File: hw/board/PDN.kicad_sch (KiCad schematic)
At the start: 40 parts, among them U1 XC7A35T-FTG256

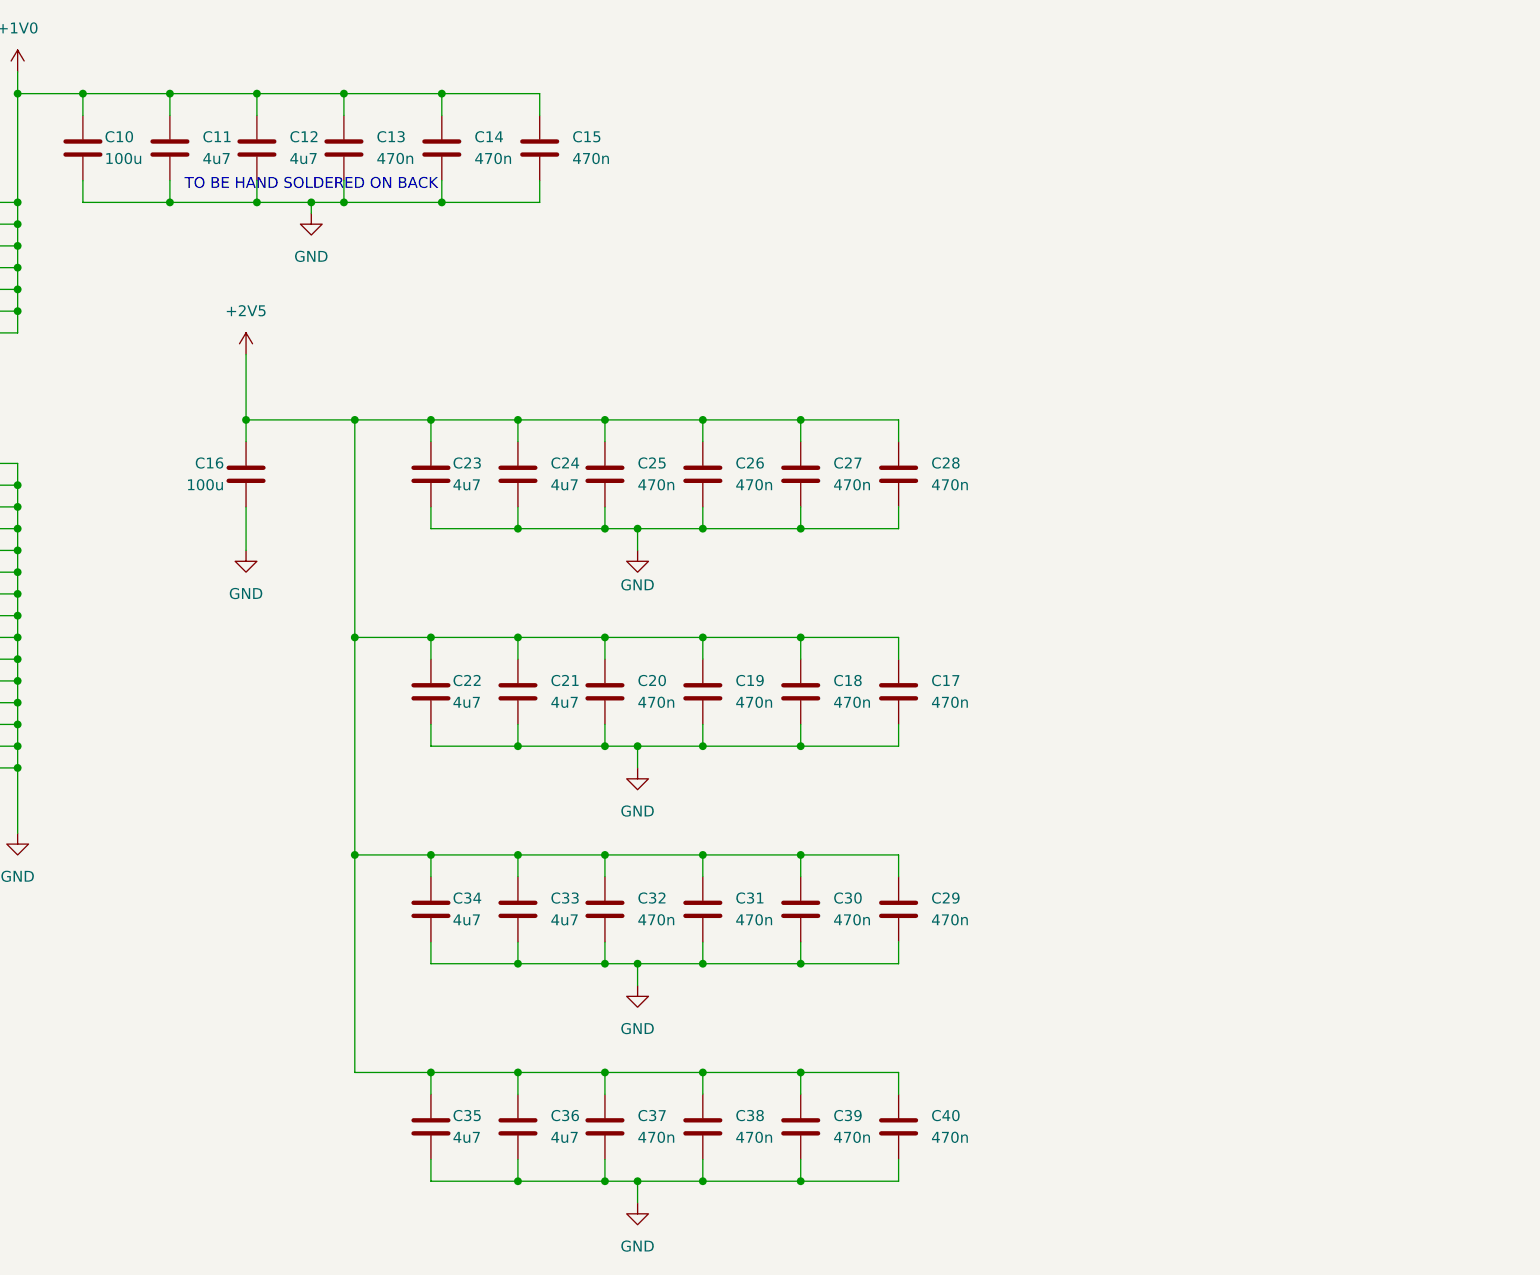
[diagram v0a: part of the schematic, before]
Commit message: Routed DE-9 connectors
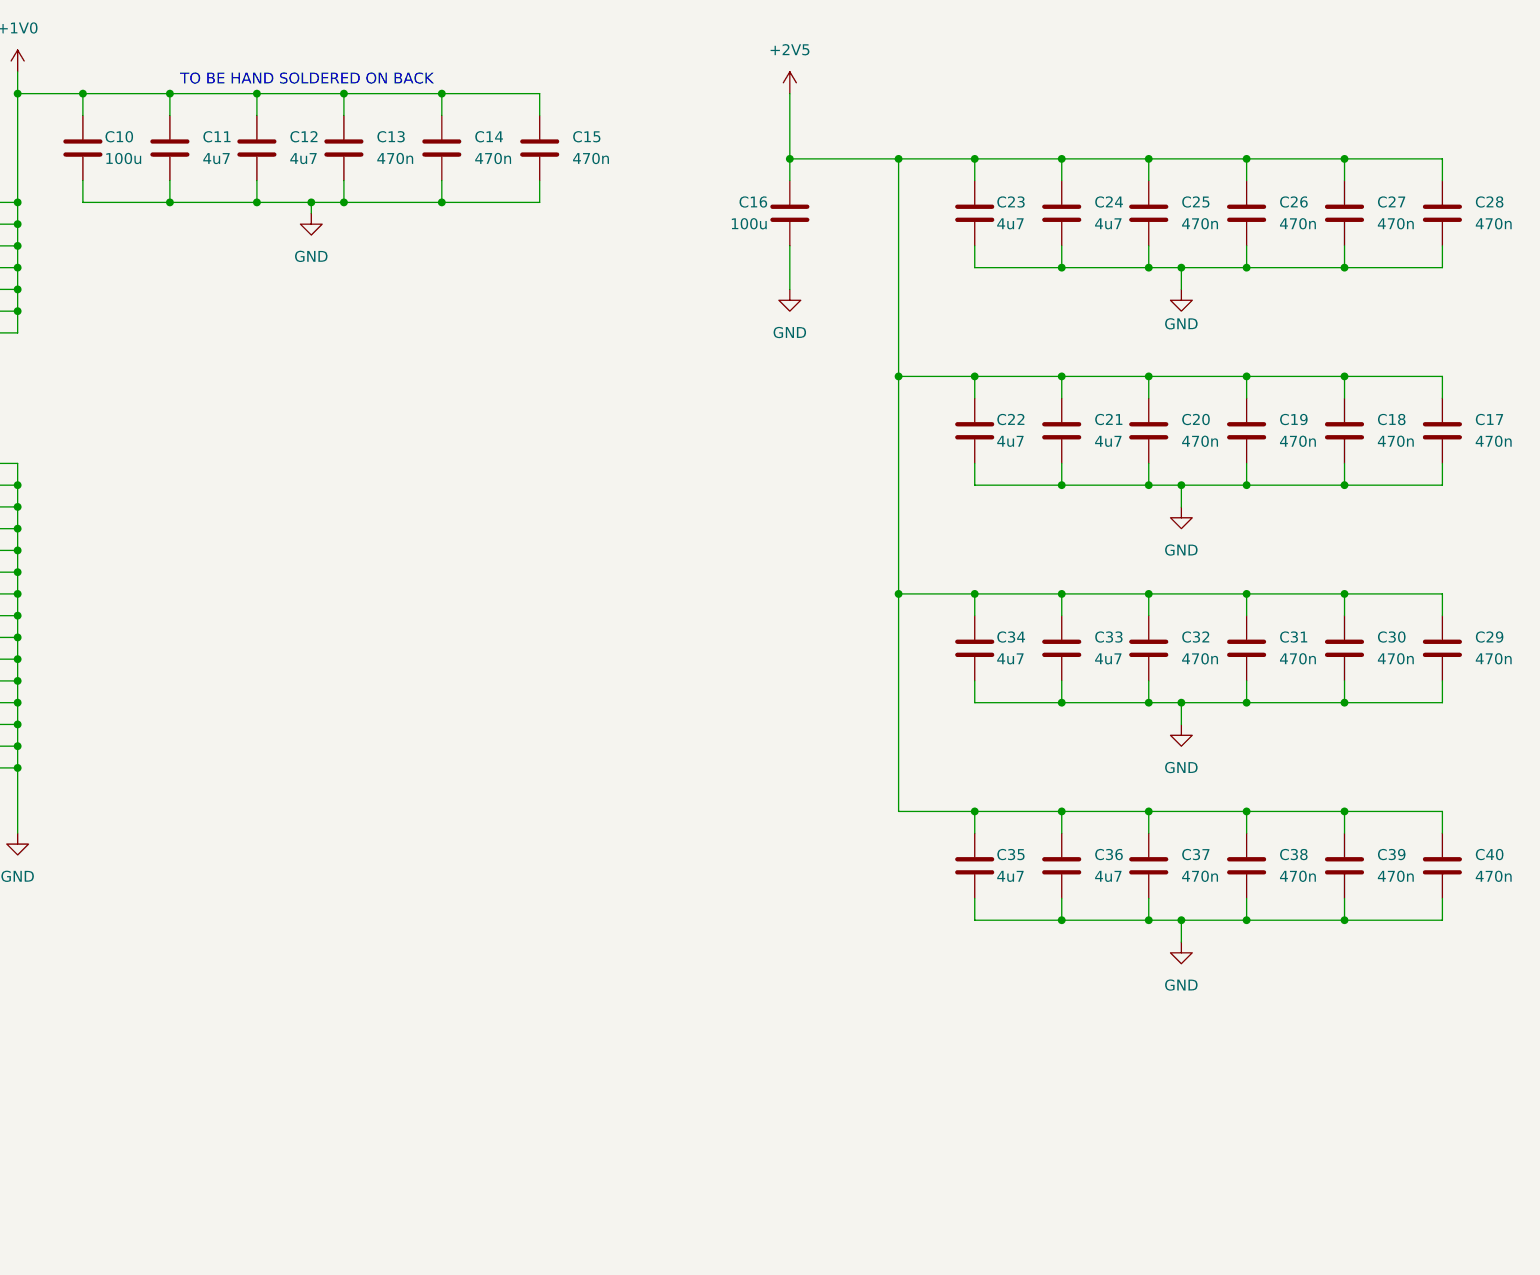
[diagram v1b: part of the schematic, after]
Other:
- moved on the sheet: C16, C17, C18, C19, C20, C21, C22, C23, C24, C25, C26, C27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

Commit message: Began routing decoupling network
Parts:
- C17, C18, C19, C20, C21, C22, C23, C24, C25, C26, C27, C28: footprint Capacitor_SMD:C_0805_2012Metric -> Capacitor_SMD:C_0805_2012Metric_Pad1.18x1.45mm_HandSolder
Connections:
- net +2V5: no longer C17.1, C18.1, C19.1, C20.1, C21.1, C22.1, C23.1, C24.1, C25.1, C26.1, C27.1, C28.1, C29.1, C30.1, C31.1, C32.1, C33.1, C34.1
- new net VCCO_14: C29.1, C30.1, C31.1, C32.1, C33.1, C34.1
- new net VCCO_15: C17.1, C18.1, C19.1, C20.1, C21.1, C22.1
- new net VCCO_35: C23.1, C24.1, C25.1, C26.1, C27.1, C28.1
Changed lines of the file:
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@@
 	)
 	(junction
-		(at 262.89 83.82)
-		(diameter 0)
-		(color 0 0 0 0)
-	)
-	(junction
 		(at 151.13 43.18)
 		(diameter 0)
@@
 	)
 	(junction
-		(at 254 58.42)
-		(diameter 0)
-		(color 0 0 0 0)
-	)
-	(junction
 		(at 87.63 43.18)
 		(diameter 0)
@@
 	)
 	(junction
-		(at 262.89 33.02)
-		(diameter 0)
-		(color 0 0 0 0)
-	)
-	(junction
 		(at 294.64 58.42)
 		(diameter 0)
@@
 	)
 	(junction
-		(at 262.89 58.42)
-		(diameter 0)
-		(color 0 0 0 0)
-	)
-	(junction
 		(at 151.13 104.14)
 		(diameter 0)
@@
 	)
 	(junction
-		(at 254 83.82)
-		(diameter 0)
-		(color 0 0 0 0)
-	)
-	(junction
 		(at 306.07 109.22)
 		(diameter 0)
@@
 	)
 	(junction
-		(at 254 33.02)
-		(diameter 0)
-		(color 0 0 0 0)
-	)
-	(junction
 		(at 87.63 71.12)
 		(diameter 0)
@@
 	(wire
 		(pts
-			(xy 254 33.02) (xy 254 58.42)
-		)
-		(stroke
-			(width 0)
-			(type default)
-		)
-	)
-	(wire
-		(pts
 			(xy 87.63 73.66) (xy 87.63 76.2)
 		)
@@
 	(wire
 		(pts
-			(xy 254 33.02) (xy 262.89 33.02)
-		)
-		(stroke
-			(width 0)
-			(type default)
-		)
-	)
-	(wire
-		(pts
 			(xy 212.09 35.56) (xy 212.09 38.1)
 		)
@@
 	(wire
 		(pts
-			(xy 254 83.82) (xy 262.89 83.82)
-		)
-		(stroke
-			(width 0)
-			(type default)
-		)
-	)
-	(wire
-		(pts
 			(xy 294.64 121.92) (xy 287.02 121.92)
 		)
@@
 	(wire
 		(pts
-			(xy 262.89 58.42) (xy 254 58.42)
-		)
-		(stroke
-			(width 0)
-			(type default)
-		)
-	)
-	(wire
-		(pts
 			(xy 25.4 38.1) (xy 36.83 38.1)
 		)
@@
 	(wire
 		(pts
-			(xy 254 83.82) (xy 254 109.22)
-		)
-		(stroke
-			(width 0)
-			(type default)
-		)
-	)
-	(wire
-		(pts
 			(xy 151.13 91.44) (xy 151.13 88.9)
 		)
@@
 	(wire
 		(pts
-			(xy 254 58.42) (xy 254 83.82)
+			(xy 254 33.02) (xy 254 109.22)
 		)
 		(stroke
@@
 		)
 	)
+	(global_label "VCCO_35"
+		(shape input)
+		(at 317.5 33.02 0)
+		(fields_autoplaced yes)
+		(effects
+			(font
+				(size 1.27 1.27)
+			)
+			(justify left)
+		)
+		(property "Intersheetrefs" "${INTERSHEET_REFS}"
+			(at 328.8309 33.02 0)
+			(effects
+				(font
+					(size 1.27 1.27)
+				)
+				(justify left)
+				(hide yes)
+			)
+		)
+	)
+	(global_label "VCCO_14"
+		(shape input)
+		(at 317.5 83.82 0)
+		(fields_autoplaced yes)
+		(effects
+			(font
+				(size 1.27 1.27)
+			)
+			(justify left)
+		)
+		(property "Intersheetrefs" "${INTERSHEET_REFS}"
+			(at 328.8309 83.82 0)
+			(effects
+				(font
+					(size 1.27 1.27)
+				)
+				(justify left)
+				(hide yes)
+			)
+		)
+	)
+	(global_label "VCCO_15"
+		(shape input)
+		(at 317.5 58.42 0)
+		(fields_autoplaced yes)
+		(effects
+			(font
+				(size 1.27 1.27)
+			)
+			(justify left)
+		)
+		(property "Intersheetrefs" "${INTERSHEET_REFS}"
+			(at 328.8309 58.42 0)
+			(effects
+				(font
+					(size 1.27 1.27)
+				)
+				(justify left)
+				(hide yes)
+			)
+		)
+	)
 	(symbol
 		(lib_id "Device:C")
@@
 			)
 		)
-		(property "Footprint" "Capacitor_SMD:C_0805_2012Metric"
+		(property "Footprint" "Capacitor_SMD:C_0805_2012Metric_Pad1.18x1.45mm_HandSolder"
 			(at 274.0152 68.58 0)
 			(effects
@@
 			)
 		)
-		(property "Footprint" "Capacitor_SMD:C_0805_2012Metric"
+		(property "Footprint" "Capacitor_SMD:C_0805_2012Metric_Pad1.18x1.45mm_HandSolder"
 			(at 274.0152 43.18 0)
 			(effects
@@
 			)
 		)
-		(property "Footprint" "Capacitor_SMD:C_0805_2012Metric"
+		(property "Footprint" "Capacitor_SMD:C_0805_2012Metric_Pad1.18x1.45mm_HandSolder"
 			(at 263.8552 68.58 0)
 			(effects
@@
 			)
 		)
-		(property "Footprint" "Capacitor_SMD:C_0805_2012Metric"
+		(property "Footprint" "Capacitor_SMD:C_0805_2012Metric_Pad1.18x1.45mm_HandSolder"
 			(at 307.0352 43.18 0)
 			(effects
@@
 			)
 		)
-		(property "Footprint" "Capacitor_SMD:C_0805_2012Metric"
+		(property "Footprint" "Capacitor_SMD:C_0805_2012Metric_Pad1.18x1.45mm_HandSolder"
 			(at 318.4652 43.18 0)
 			(effects
@@
 			)
 		)
-		(property "Footprint" "Capacitor_SMD:C_0805_2012Metric"
+		(property "Footprint" "Capacitor_SMD:C_0805_2012Metric_Pad1.18x1.45mm_HandSolder"
 			(at 284.1752 68.58 0)
 			(effects
@@
 			)
 		)
-		(property "Footprint" "Capacitor_SMD:C_0805_2012Metric"
+		(property "Footprint" "Capacitor_SMD:C_0805_2012Metric_Pad1.18x1.45mm_HandSolder"
 			(at 318.4652 68.58 0)
 			(effects
@@
 			)
 		)
-		(property "Footprint" "Capacitor_SMD:C_0805_2012Metric"
+		(property "Footprint" "Capacitor_SMD:C_0805_2012Metric_Pad1.18x1.45mm_HandSolder"
 			(at 295.6052 43.18 0)
 			(effects
@@
 			)
 		)
-		(property "Footprint" "Capacitor_SMD:C_0805_2012Metric"
+		(property "Footprint" "Capacitor_SMD:C_0805_2012Metric_Pad1.18x1.45mm_HandSolder"
 			(at 284.1752 43.18 0)
 			(effects
@@
 			)
 		)
-		(property "Footprint" "Capacitor_SMD:C_0805_2012Metric"
+		(property "Footprint" "Capacitor_SMD:C_0805_2012Metric_Pad1.18x1.45mm_HandSolder"
 			(at 307.0352 68.58 0)
 			(effects
@@
 			)
 		)
-		(property "Footprint" "Capacitor_SMD:C_0805_2012Metric"
+		(property "Footprint" "Capacitor_SMD:C_0805_2012Metric_Pad1.18x1.45mm_HandSolder"
 			(at 295.6052 68.58 0)
 			(effects
@@
 			)
 		)
-		(property "Footprint" "Capacitor_SMD:C_0805_2012Metric"
+		(property "Footprint" "Capacitor_SMD:C_0805_2012Metric_Pad1.18x1.45mm_HandSolder"
 			(at 263.8552 43.18 0)
 			(effects

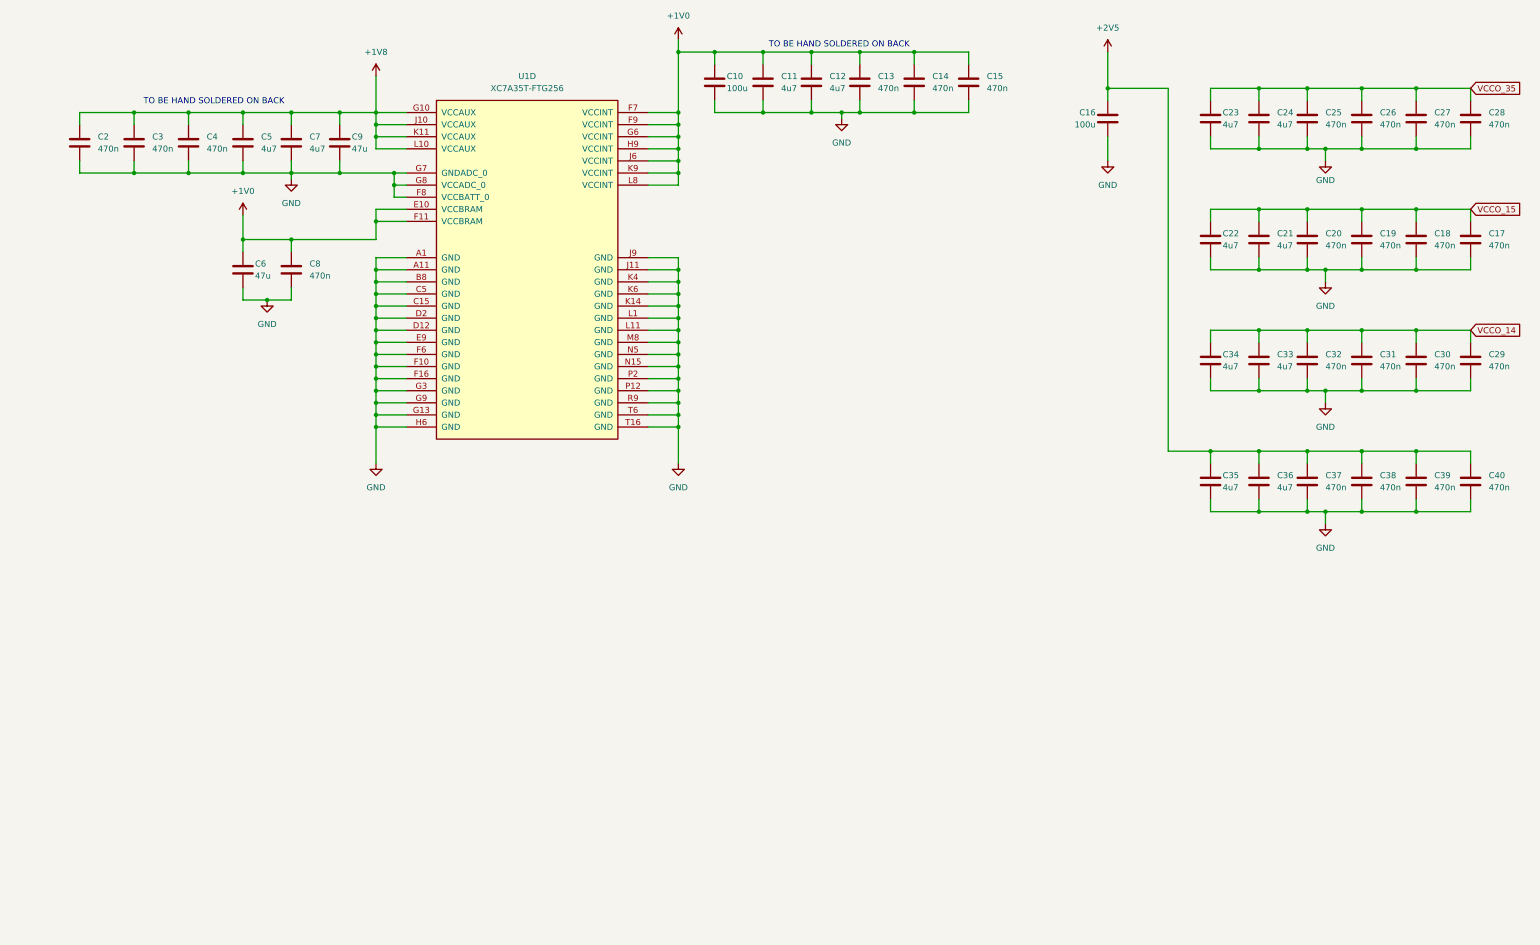
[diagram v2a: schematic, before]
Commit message: Added TPS54331 regulator schematic for 2v5 delivery
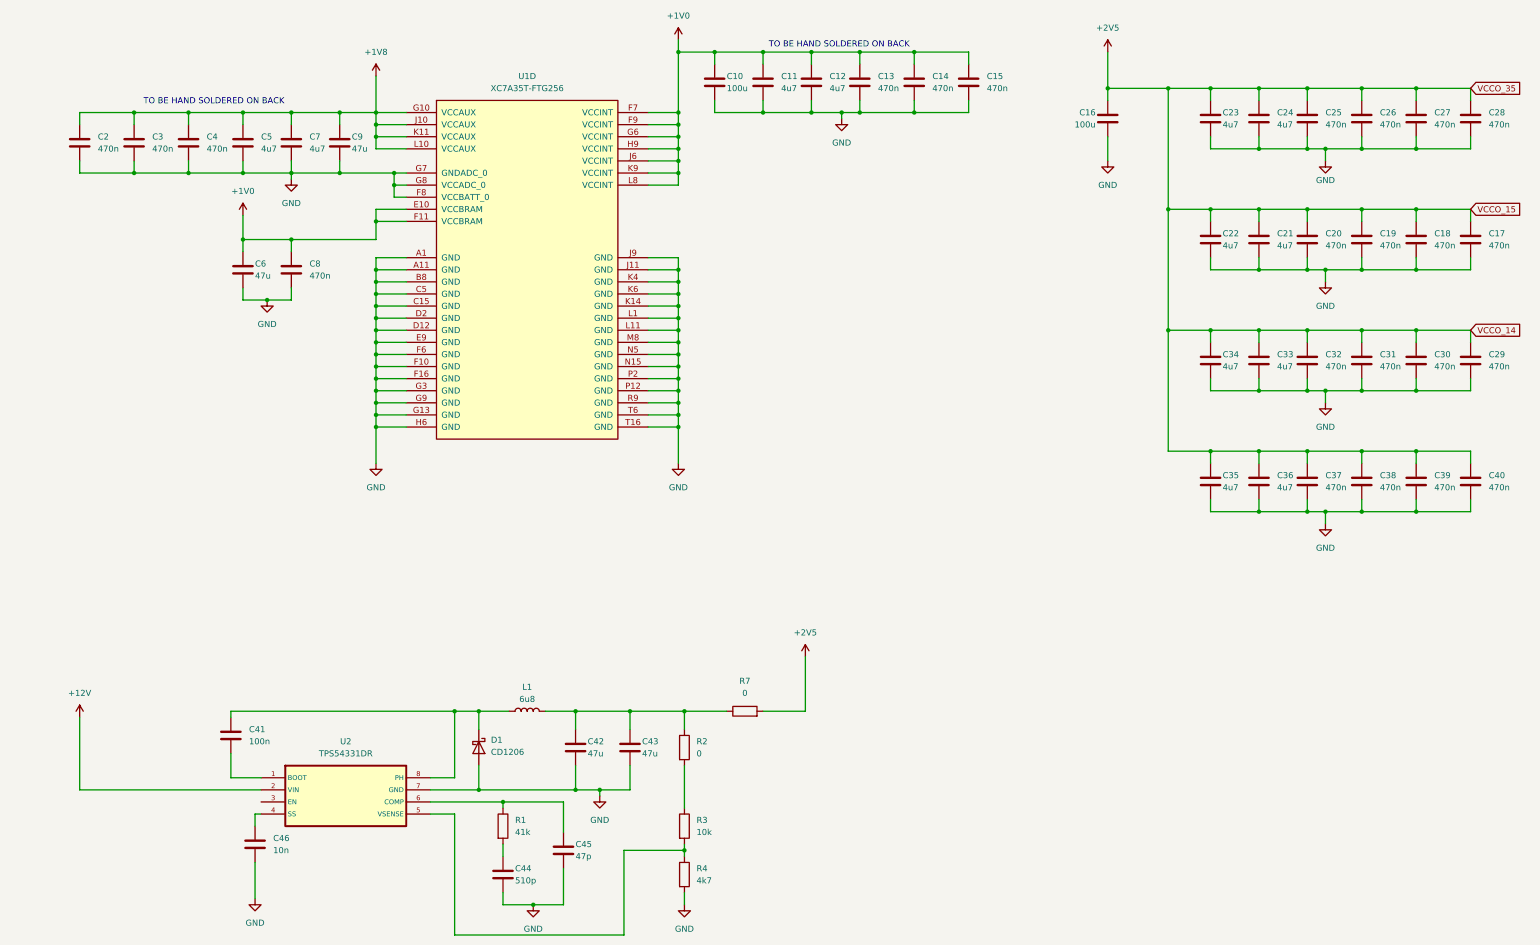
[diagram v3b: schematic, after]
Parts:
- added C41: 100n, Capacitor_SMD:C_0805_2012Metric_Pad1.18x1.45mm_HandSolder, symbol Device:C
- added C42, C43: 47u, Capacitor_SMD:C_0805_2012Metric_Pad1.18x1.45mm, symbol Device:C
- added C44: 510p, Capacitor_SMD:C_0805_2012Metric, symbol Device:C
- added C45: 47p, Capacitor_SMD:C_0805_2012Metric_Pad1.18x1.45mm, symbol Device:C
- added C46: 10n, Capacitor_SMD:C_0805_2012Metric_Pad1.18x1.45mm, symbol Device:C
- added D1: CD1206, Diode_SMD:D_1206_3216Metric, symbol Device:D_Schottky
- added L1: 6u8, Inductor_SMD:L_1206_3216Metric, symbol Device:L
- added R1: 41k, Resistor_SMD:R_0805_2012Metric, symbol Device:R
- added R2, R7: 0, Resistor_SMD:R_0805_2012Metric, symbol Device:R
- added R3: 10k, Resistor_SMD:R_0805_2012Metric, symbol Device:R
- added R4: 4k7, Resistor_SMD:R_0805_2012Metric, symbol Device:R
- added U2: TPS54331DR, Snapeda:SOIC127P599X175-8N, symbol Snapeda:TPS54331DR
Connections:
- net VCCO_14 is gone; now on net +2V5: C29.1, C30.1, C31.1, C32.1, C33.1, C34.1
- net VCCO_15 is gone; now on net +2V5: C17.1, C18.1, C19.1, C20.1, C21.1, C22.1
- net VCCO_35 is gone; now on net +2V5: C23.1, C24.1, C25.1, C26.1, C27.1, C28.1
- net +2V5: now also R7.2
- net GND: now also C42.2, C43.2, C44.2, C45.2, C46.2, D1.2 (A), R4.2, U2.7 (GND)
- new net: C42.1, C43.1, L1.2, R2.1, R7.1
- new net: R2.2, R3.1
- new net: C45.1, R1.1, U2.6 (COMP)
- new net: R3.2, R4.1, U2.5 (VSENSE)
- new net: C44.1, R1.2
- new net: C41.1, D1.1 (K), L1.1, U2.8 (PH)
- new net: C41.2, U2.1 (BOOT)
- new net: C46.1, U2.4 (SS)
- new net +12V: U2.2 (VIN)

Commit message: Routed decoupling capacitors
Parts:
- removed C15, C17, C18, C2, C27, C28: 470n, Capacitor_SMD:C_0805_2012Metric_Pad1.18x1.45mm_HandSolder, symbol Device:C
- removed C29, C30, C38, C39, C40: 470n, Capacitor_SMD:C_0805_2012Metric, symbol Device:C
- C10, C11, C12, C13, C14, C16, C19, C20, C21, C22, C23, C24, C25, C26, C3, C4, C41, C5, C6, C7, C8, C9: footprint Capacitor_SMD:C_0805_2012Metric_Pad1.18x1.45mm_HandSolder -> Capacitor_SMD:C_0805_2012Metric
- C42, C43, C45, C46: footprint Capacitor_SMD:C_0805_2012Metric_Pad1.18x1.45mm -> Capacitor_SMD:C_0805_2012Metric
- L1: footprint Inductor_SMD:L_1206_3216Metric -> Inductor_SMD:L_Chilisin_BMRF00101040
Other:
- note removed: "TO BE HAND SOLDERED ON BACK"

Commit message: Routed all voltage regulators
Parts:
- added C2: 47u, Capacitor_SMD:C_0805_2012Metric, symbol Device:C
- added U3: AP7361C-18SP-13, Package_SO:SOIC-8-1EP_3.9x4.9mm_P1.27mm_EP2.41x3.3mm_ThermalVias, symbol DE9:AP7361C-18SP-13
- added U4: AP7361C-10E, Package_TO_SOT_SMD:SOT-223-3_TabPin2, symbol Regulator_Linear:AP7361C-10E
- C12: value 4u7 -> 47u
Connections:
- net +1V0: now also U4.3 (VO); no longer C12.1
- net +1V8: now also U3.1 (VO)
- net +2V5: now also C12.1, C2.1, U3.2 (EN), U3.8 (VI), U4.1 (VI)
- net GND: now also C2.2, U3.4 (GND), U4.2 (GND)
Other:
- moved on the sheet: C13, C14
